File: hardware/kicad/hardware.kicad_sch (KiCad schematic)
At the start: 0 parts

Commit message: power management
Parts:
- added C1: 1u, Capacitor_SMD:C_0805_2012Metric, symbol Device:C_Small
- added C2: 10u, Capacitor_SMD:C_0805_2012Metric, symbol Device:C_Small
- added J1: Conn_01x02_Pin, Connector_JST:JST_PH_B2B-PH-K_1x02_P2.00mm_Vertical, symbol Connector:Conn_01x02_Pin
- added J2: USB_C_Receptacle_USB2.0_14P, Connector_USB:USB_C_Receptacle_HRO_TYPE-C-31-M-12, symbol Connector:USB_C_Receptacle_USB2.0_14P
- added R1, R2: 5.1k, Resistor_SMD:R_0805_2012Metric, symbol Device:R
- added R3: 3.3k, Resistor_SMD:R_0805_2012Metric, symbol Device:R
- added R4: 10k, Resistor_SMD:R_0805_2012Metric, symbol Device:R
- added U1: STM32L412CBTx, Package_QFP:LQFP-48_7x7mm_P0.5mm, symbol MCU_ST_STM32L4:STM32L412CBTx
- added U2: BQ24074RGT, Package_DFN_QFN:VQFN-16-1EP_3x3mm_P0.5mm_EP1.6x1.6mm, symbol Battery_Management:BQ24074RGT
- added U3: NCP163AFCT330T2G, Package_CSP:WLCSP-4_0.64x0.64mm_Layout2x2_P0.35mm, symbol Regulator_Linear:NCP163AFCT330T2G
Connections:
- new net: J2.A7 (D-), J2.B7 (D-), U1.32 (PA11)
- new net: J2.A6 (D+), J2.B6 (D+), U1.33 (PA12)
- new net: C1.1, J2.A4 (VBUS), J2.A9 (VBUS), J2.B4 (VBUS), J2.B9 (VBUS), U1.36 (VDDUSB), U2.13 (IN)
- new net: R3.1, U2.12 (ILIM)
- new net: J2.B5 (CC2), R2.1
- new net: C2.1, J1.1 (Pin_1), U2.2 (BAT), U2.3 (BAT)
- new net: R4.2, U2.1 (TS)
- new net: J2.A5 (CC1), R1.1
- new net +3.3V: U1.1 (VBAT), U1.24 (VDD), U1.48 (VDD), U1.9 (VDDA), U2.6 (EN1), U3.A2 (VOUT), U3.B1 (EN)
- new net +4V: U2.10 (OUT), U2.11 (OUT), U3.A1 (VIN)
- new net GND: C1.2, C2.2, J1.2 (Pin_2), J2.A1 (GND), J2.A12 (GND), J2.B1 (GND), J2.B12 (GND), J2.SH (SHIELD), R1.2, R2.2, R3.2, R4.1, U1.23 (VSS), U1.35 (VSS), U1.47 (VSS), U1.8 (VSSA), U2.17 (VSS), U2.4 (~{CE}), U2.5 (EN2), U2.8 (VSS), U3.B2 (GND)

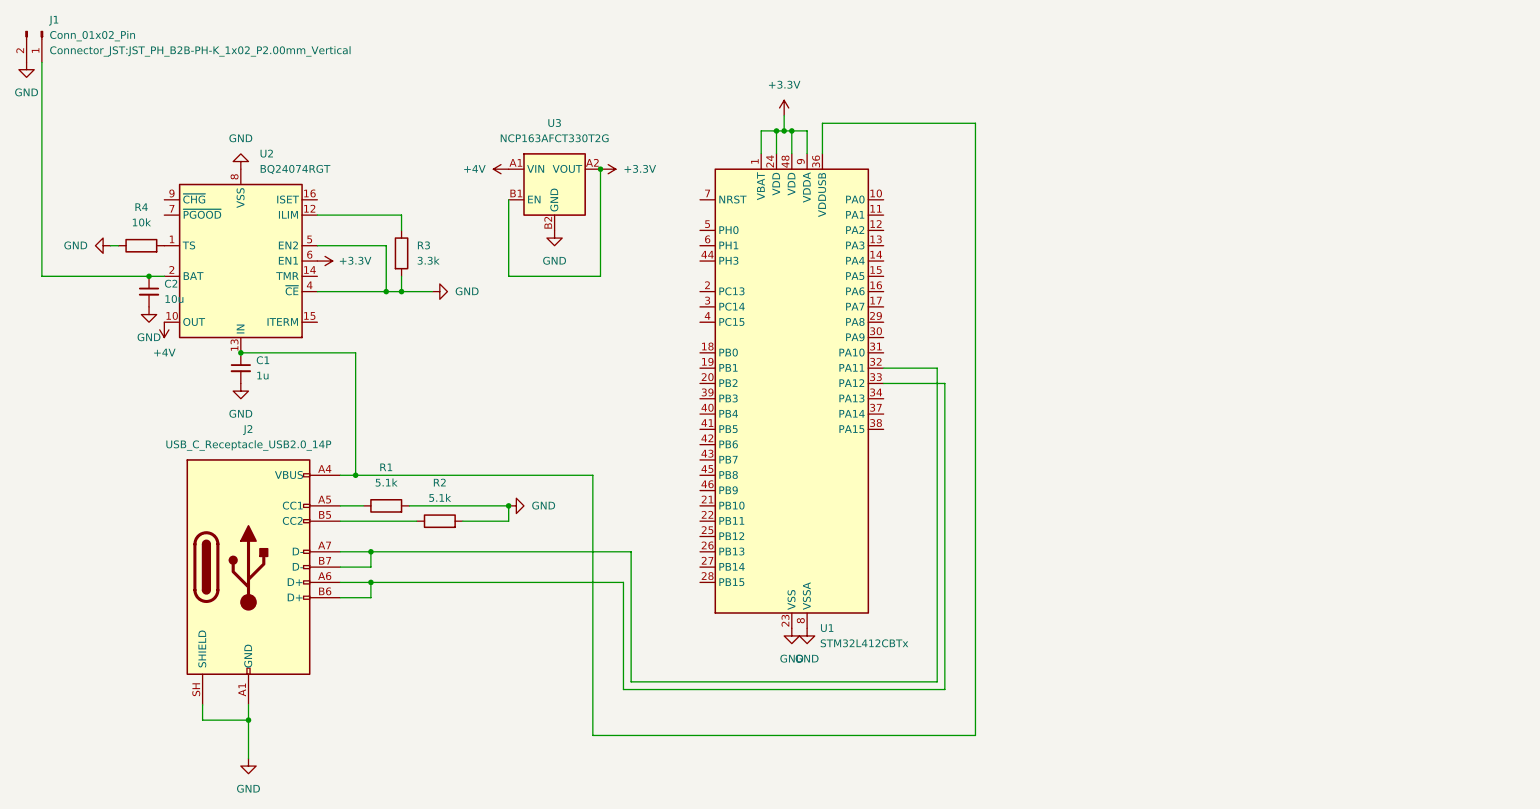
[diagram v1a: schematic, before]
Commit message: connect gps receiver and add sd card slot
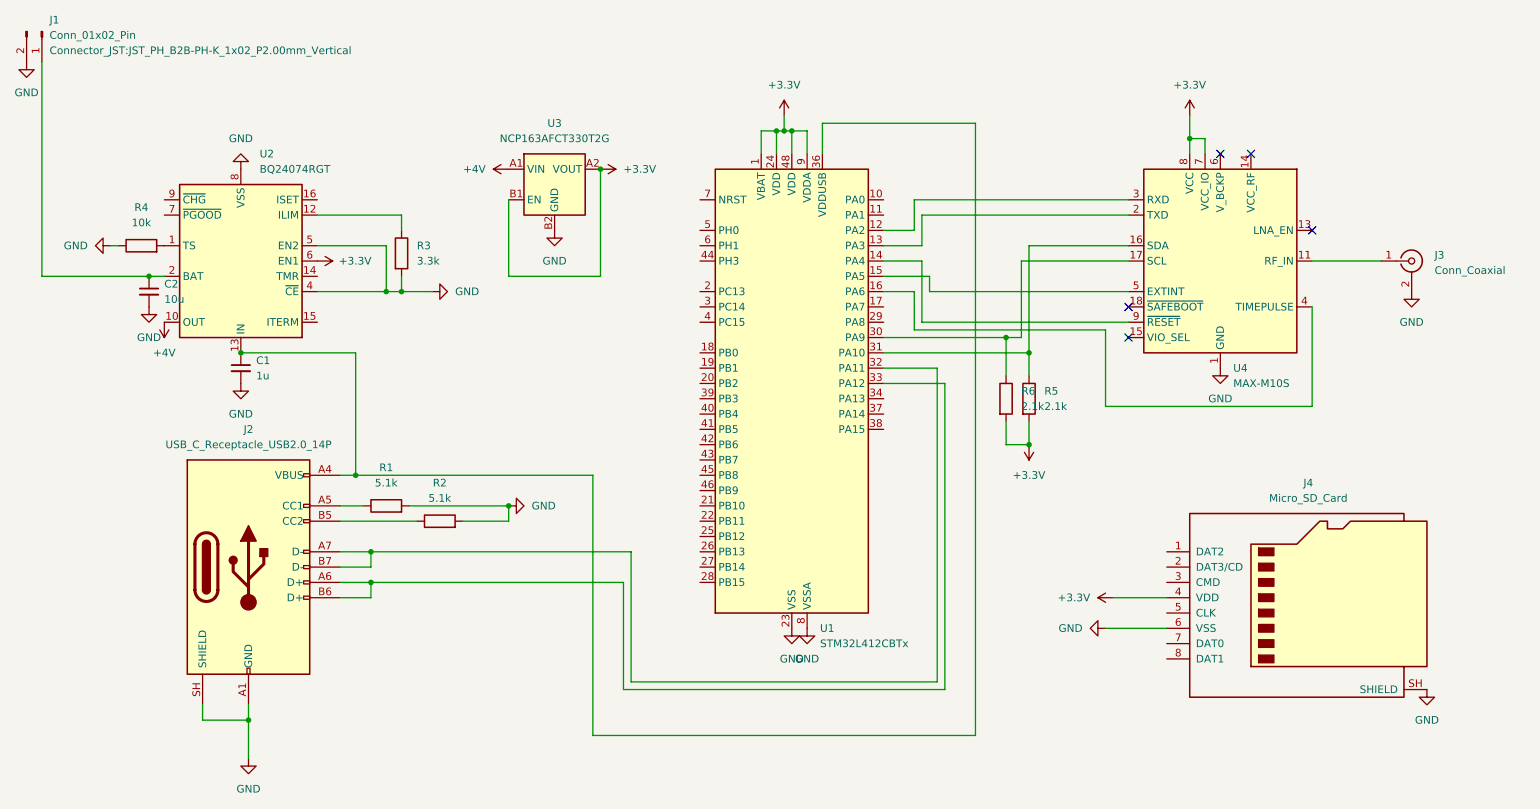
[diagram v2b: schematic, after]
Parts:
- added J3: Conn_Coaxial, Connector_Coaxial:U.FL_Hirose_U.FL-R-SMT-1_Vertical, symbol Connector:Conn_Coaxial
- added J4: Micro_SD_Card, Connector_Card:microSD_HC_Hirose_DM3AT-SF-PEJM5, symbol Connector:Micro_SD_Card
- added R5, R6: 2.1k, Resistor_SMD:R_0805_2012Metric_Pad1.20x1.40mm_HandSolder, symbol Device:R
- added U4: MAX-M10S, RF_GPS:ublox_MAX, symbol RF_GPS:MAX-M10S
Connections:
- net +3.3V: now also J4.4 (VDD), R5.2, R6.2, U4.7 (VCC_IO), U4.8 (VCC)
- net GND: now also J3.2 (Ext), J4.6 (VSS), J4.SH (SHIELD), U4.1 (GND), U4.10 (GND), U4.12 (GND)
- net at U1.12 (PA2): now also U4.3 (RXD)
- net at U1.13 (PA3): now also U4.2 (TXD)
- net at U1.14 (PA4): now also U4.9 (~{RESET})
- net at U1.15 (PA5): now also U4.5 (EXTINT)
- net at U1.16 (PA6): now also U4.4 (TIMEPULSE)
- net at U1.30 (PA9): now also R6.1, U4.17 (SCL)
- net at U1.31 (PA10): now also R5.1, U4.16 (SDA)
- new net: J3.1 (In), U4.11 (RF_IN)
- no-connect marks 0 -> 5

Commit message: reroute main pcb
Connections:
- net at U1.25 (PB12): now also J4.2 (DAT3/CD)
- net at U1.26 (PB13): now also J4.5 (CLK)
- net at U1.27 (PB14): now also J4.7 (DAT0)
- net at U1.28 (PB15): now also J4.3 (CMD)
- no-connect marks 5 -> 7
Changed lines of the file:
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@@
 	)
 	(no_connect
+		(at 227.33 113.03)
+	)
+	(no_connect
 		(at 220.98 77.47)
 	)
@@
 		(at 251.46 59.69)
 	)
+	(no_connect
+		(at 227.33 130.81)
+	)
 	(wire
 		(pts
@@
 	(wire
 		(pts
+			(xy 196.85 123.19) (xy 227.33 123.19)
+		)
+		(stroke
+			(width 0)
+			(type default)
+		)
+	)
+	(wire
+		(pts
 			(xy 233.68 44.45) (xy 233.68 46.99)
 		)
@@
 	(wire
 		(pts
-			(xy 132.08 100.33) (xy 132.08 143.51)
+			(xy 132.08 100.33) (xy 132.08 142.24)
 		)
 		(stroke
@@
 	(wire
 		(pts
+			(xy 144.78 137.16) (xy 196.85 137.16)
+		)
+		(stroke
+			(width 0)
+			(type default)
+		)
+	)
+	(wire
+		(pts
 			(xy 100.33 57.15) (xy 100.33 59.69)
 		)
@@
 	(wire
 		(pts
+			(xy 147.32 139.7) (xy 147.32 118.11)
+		)
+		(stroke
+			(width 0)
+			(type default)
+		)
+	)
+	(wire
+		(pts
 			(xy 186.69 62.23) (xy 180.34 62.23)
 		)
@@
 	(wire
 		(pts
+			(xy 194.31 138.43) (xy 146.05 138.43)
+		)
+		(stroke
+			(width 0)
+			(type default)
+		)
+	)
+	(wire
+		(pts
 			(xy 40.64 67.31) (xy 58.42 67.31)
 		)
@@
 	(wire
 		(pts
+			(xy 191.77 115.57) (xy 191.77 140.97)
+		)
+		(stroke
+			(width 0)
+			(type default)
+		)
+	)
+	(wire
+		(pts
 			(xy 217.17 125.73) (xy 227.33 125.73)
 		)
@@
 	(wire
 		(pts
+			(xy 193.04 139.7) (xy 147.32 139.7)
+		)
+		(stroke
+			(width 0)
+			(type default)
+		)
+	)
+	(wire
+		(pts
+			(xy 147.32 118.11) (xy 149.86 118.11)
+		)
+		(stroke
+			(width 0)
+			(type default)
+		)
+	)
+	(wire
+		(pts
 			(xy 217.17 88.9) (xy 217.17 76.2)
 		)
@@
 	(wire
 		(pts
+			(xy 143.51 110.49) (xy 149.86 110.49)
+		)
+		(stroke
+			(width 0)
+			(type default)
+		)
+	)
+	(wire
+		(pts
+			(xy 146.05 138.43) (xy 146.05 115.57)
+		)
+		(stroke
+			(width 0)
+			(type default)
+		)
+	)
+	(wire
+		(pts
 			(xy 58.42 67.31) (xy 60.96 67.31)
 		)
@@
 	(wire
 		(pts
+			(xy 191.77 140.97) (xy 143.51 140.97)
+		)
+		(stroke
+			(width 0)
+			(type default)
+		)
+	)
+	(wire
+		(pts
 			(xy 251.46 64.77) (xy 262.89 64.77)
 		)
@@
 	(wire
 		(pts
+			(xy 227.33 128.27) (xy 194.31 128.27)
+		)
+		(stroke
+			(width 0)
+			(type default)
+		)
+	)
+	(wire
+		(pts
 			(xy 90.17 107.95) (xy 102.87 107.95)
 		)
@@
 	(wire
 		(pts
+			(xy 143.51 140.97) (xy 143.51 110.49)
+		)
+		(stroke
+			(width 0)
+			(type default)
+		)
+	)
+	(wire
+		(pts
 			(xy 90.17 118.11) (xy 95.25 118.11)
 		)
@@
 	(wire
 		(pts
+			(xy 149.86 113.03) (xy 144.78 113.03)
+		)
+		(stroke
+			(width 0)
+			(type default)
+		)
+	)
+	(wire
+		(pts
 			(xy 138.43 113.03) (xy 138.43 134.62)
 		)
@@
 	(wire
 		(pts
+			(xy 144.78 113.03) (xy 144.78 137.16)
+		)
+		(stroke
+			(width 0)
+			(type default)
+		)
+	)
+	(wire
+		(pts
 			(xy 100.33 67.31) (xy 100.33 69.85)
 		)
@@
 	(wire
 		(pts
+			(xy 146.05 115.57) (xy 149.86 115.57)
+		)
+		(stroke
+			(width 0)
+			(type default)
+		)
+	)
+	(wire
+		(pts
+			(xy 193.04 118.11) (xy 193.04 139.7)
+		)
+		(stroke
+			(width 0)
+			(type default)
+		)
+	)
+	(wire
+		(pts
 			(xy 110.49 107.95) (xy 118.11 107.95)
 		)
@@
 	(wire
 		(pts
+			(xy 227.33 118.11) (xy 193.04 118.11)
+		)
+		(stroke
+			(width 0)
+			(type default)
+		)
+	)
+	(wire
+		(pts
 			(xy 189.23 134.62) (xy 189.23 82.55)
 		)
@@
 	(wire
 		(pts
+			(xy 196.85 137.16) (xy 196.85 123.19)
+		)
+		(stroke
+			(width 0)
+			(type default)
+		)
+	)
+	(wire
+		(pts
 			(xy 165.1 43.18) (xy 167.64 43.18)
 		)
@@
 	(wire
 		(pts
+			(xy 227.33 115.57) (xy 191.77 115.57)
+		)
+		(stroke
+			(width 0)
+			(type default)
+		)
+	)
+	(wire
+		(pts
 			(xy 73.66 80.01) (xy 92.71 80.01)
 		)
@@
 	(wire
 		(pts
-			(xy 132.08 143.51) (xy 195.58 143.51)
+			(xy 132.08 142.24) (xy 195.58 142.24)
 		)
 		(stroke
@@
 	(wire
 		(pts
-			(xy 195.58 143.51) (xy 195.58 41.91)
+			(xy 195.58 142.24) (xy 195.58 41.91)
 		)
 		(stroke
@@
 	(wire
 		(pts
+			(xy 194.31 128.27) (xy 194.31 138.43)
+		)
+		(stroke
+			(width 0)
+			(type default)
+		)
+	)
+	(wire
+		(pts
 			(xy 74.93 140.97) (xy 74.93 147.32)
 		)
@@
 		(in_pos_files yes)
 		(dnp no)
-		(fields_autoplaced yes)
 		(property "Reference" "R6"
-			(at 203.2 86.3599 0)
+			(at 196.342 85.344 0)
 			(show_name no)
 			(do_not_autoplace no)
@@
 		)
 		(property "Value" "2.1k"
-			(at 203.2 88.8999 0)
+			(at 196.596 88.9 0)
 			(show_name no)
 			(do_not_autoplace no)
